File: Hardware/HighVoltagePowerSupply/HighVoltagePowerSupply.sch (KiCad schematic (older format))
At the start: 138 parts, among them J1 Conn_01x02_Female, J10 Conn_01x01_Male, J11 Conn_01x01_Male, J12 Conn_01x01_Male, J13 Conn_01x01_Male, J14 Conn_01x01_Male, J15 Conn_01x03_Female, J16 Conn_01x02_Female, J2 Conn_01x01_Male, J3 Conn_01x01_Male, J4 Conn_01x01_Male, J5 Conn_01x01_Male, J6 Conn_01x01_Male, J7 Conn_01x01_Male, J8 Conn_01x01_Male, J9 Conn_01x01_Male, Q1 BC859, U1 LT3580xMS8E, U3 MCP6V51

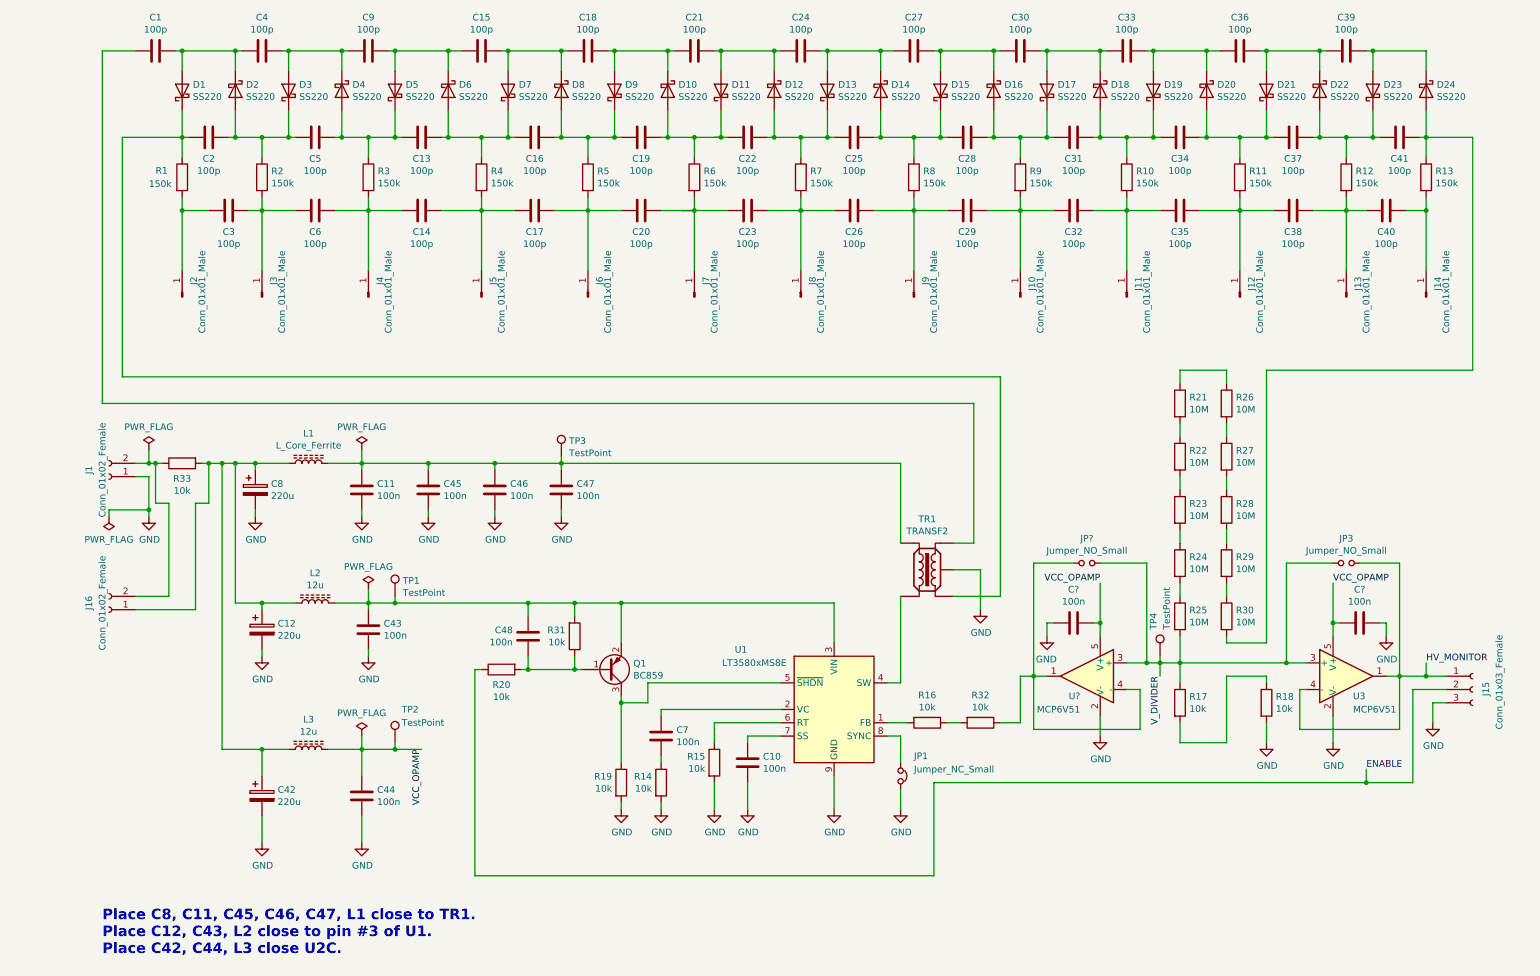
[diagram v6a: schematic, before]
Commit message: 1. GA3459-BL transformwer will be used for hv power supply, added it to the circuit (fix: #7). 2. Status of hv power supply (output voltage, temperature, input current) will be send in an analog way and won't be galvanically isolated (fix: #68) 3. Added missing footprints. 5. Removed obsolete files.
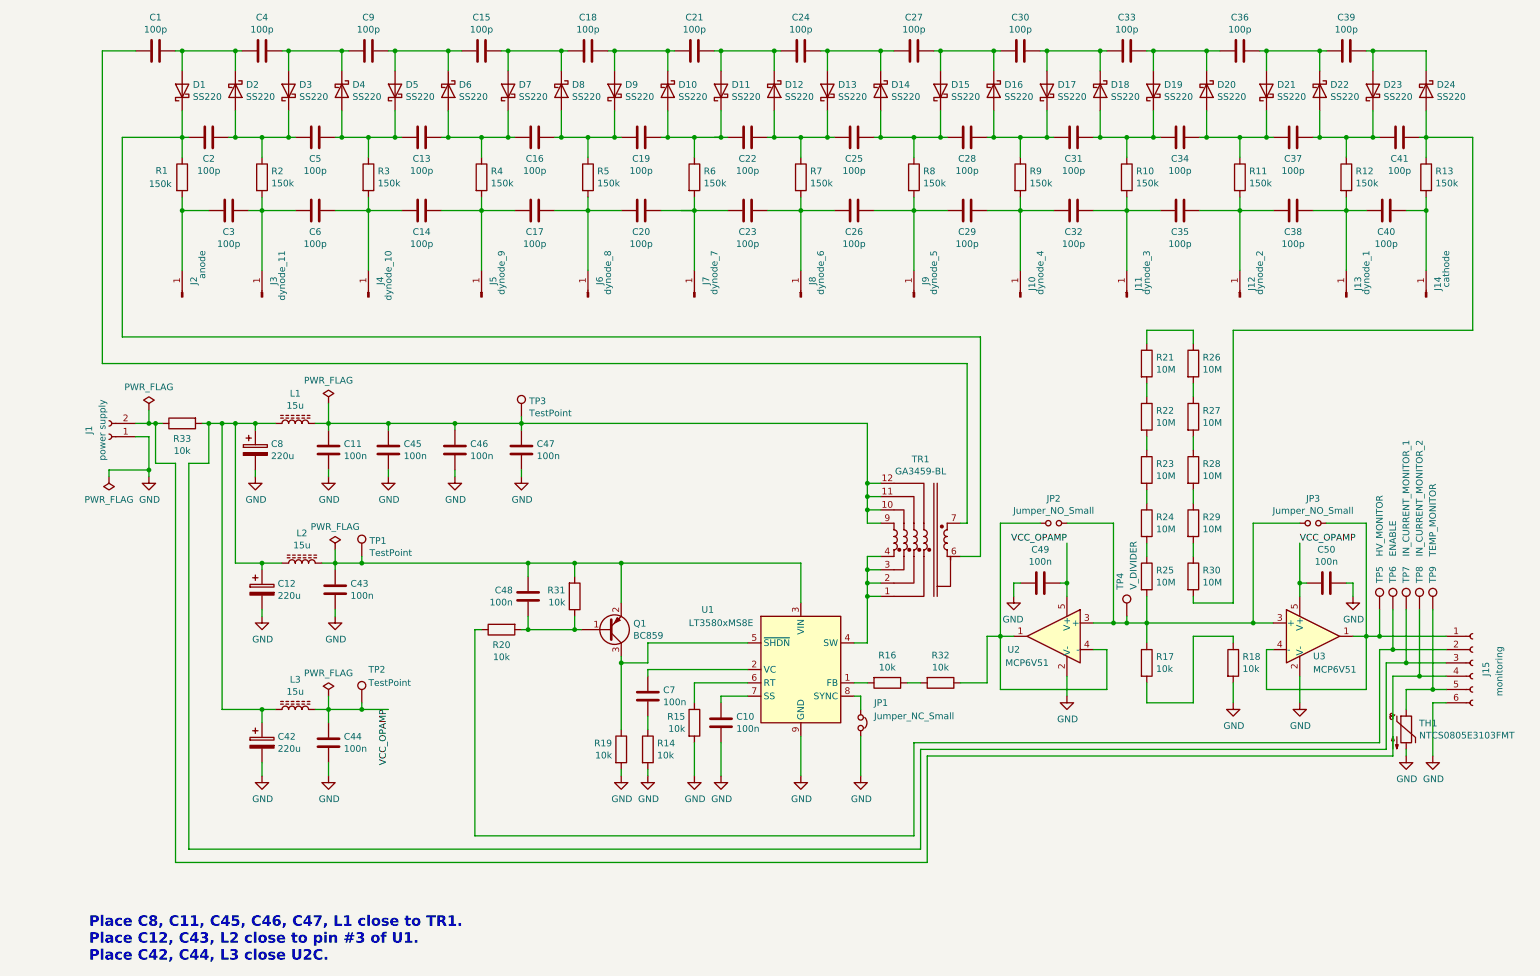
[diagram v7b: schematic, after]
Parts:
- removed J15: Conn_01x03_Female, symbol Connector:Conn_01x03_Female
- removed J16: Conn_01x02_Female, symbol Connector:Conn_01x02_Female
- removed TR1: TRANSF2, symbol Transformer:TRANSF2
- removed U?: MCP6V51, Package_TO_SOT_SMD:SOT-23-5, symbol HighVoltagePowerSupply:MCP6V51
- added J15: monitoring, Connector_PinSocket_2.54mm:PinSocket_1x06_P2.54mm_Vertical, symbol Connector:Conn_01x06_Female
- added TH1: NTCS0805E3103FMT, Resistor_SMD:R_0805_2012Metric, symbol Device:Thermistor_NTC
- added TP5: HV_MONITOR, TestPoint:TestPoint_Pad_D2.5mm, symbol Connector:TestPoint
- added TP6: ENABLE, TestPoint:TestPoint_Pad_D2.5mm, symbol Connector:TestPoint
- added TP7: IN_CURRENT_MONITOR_1, TestPoint:TestPoint_Pad_D2.5mm, symbol Connector:TestPoint
- added TP8: IN_CURRENT_MONITOR_2, TestPoint:TestPoint_Pad_D2.5mm, symbol Connector:TestPoint
- added TP9: TEMP_MONITOR, TestPoint:TestPoint_Pad_D2.5mm, symbol Connector:TestPoint
- added TR1: GA3459-BL, HighVoltagePowerSupply:GA3459-BL, symbol HighVoltagePowerSupply:GA3459-BL
- added U2: MCP6V51, Package_TO_SOT_SMD:SOT-23-5, symbol HighVoltagePowerSupply:MCP6V51
- J1: value Conn_01x02_Female -> power supply; footprint (none) -> HighVoltagePowerSupply:DG300-5.0-02P-12-00A(H)
- J10: value Conn_01x01_Male -> dynode_4
- J11: value Conn_01x01_Male -> dynode_3
- J12: value Conn_01x01_Male -> dynode_2
- J13: value Conn_01x01_Male -> dynode_1
- J14: value Conn_01x01_Male -> cathode
- J2: value Conn_01x01_Male -> anode
- J3: value Conn_01x01_Male -> dynode_11
- J4: value Conn_01x01_Male -> dynode_10
- J5: value Conn_01x01_Male -> dynode_9
- J6: value Conn_01x01_Male -> dynode_8
- J7: value Conn_01x01_Male -> dynode_7
- J8: value Conn_01x01_Male -> dynode_6
- J9: value Conn_01x01_Male -> dynode_5
- L1: value L_Core_Ferrite -> 15u; footprint DataAcquisition:L_7.3x7.3_H3.5 -> HighVoltagePowerSupply:DJNR3015-150
- L2, L3: value 12u -> 15u; footprint DataAcquisition:L_7.3x7.3_H3.5 -> HighVoltagePowerSupply:DJNR3015-150
- TP4: value TestPoint -> V_DIVIDER
- gave numbers to parts that had none: 3
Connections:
- net GND: now also J15.6 (Pin_6), TH1.2, U2.2 (V-)
- net VCC_OPAMP: now also U2.5 (V+)
- net at C1.2: now also TR1.7
- net at C2.2, D1.1 (K), R1.1: now also TR1.6
- net at JP2.2, R32.1: now also U2.1, U2.4 (-)
- net at J1.2 (Pin_2), R33.1: now also J15.4 (Pin_4), TP8.1
- net at C12.1, C42.1, C8.1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: now also J15.3 (Pin_3), TP7.1
- net at U1.4 (SW): now also TR1.1, TR1.2, TR1.3, TR1.4
- net at C11.2, C45.2, C46.2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: now also TR1.10, TR1.11, TR1.12, TR1.9
- net ENABLE: no longer names the net of R20.1
- net ENABLE: now also J15.2 (Pin_2), TP6.1
- net HV_MONITOR: no longer names the net of JP3.2, U3.1, U3.4 (-)
- net HV_MONITOR: now also J15.1 (Pin_1), TP5.1
- net V_DIVIDER: no longer names the net of JP2.1, JP3.1, R17.1, R25.2, TP4.1, U3.3 (+)
- net V_DIVIDER: now also U2.3 (+)
- new net: J15.5 (Pin_5), TH1.1, TP9.1
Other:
- moved on the sheet: C10, C11, C12, C42, C43, C44, C45, C46, C47, C48, C49, C50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

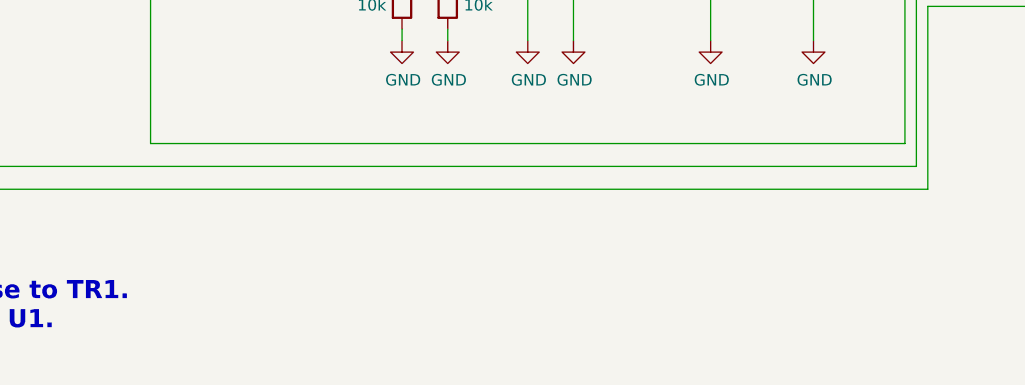
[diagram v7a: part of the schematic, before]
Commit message: Chose correct PCB outlines based on mechanical overview (fix: #50).
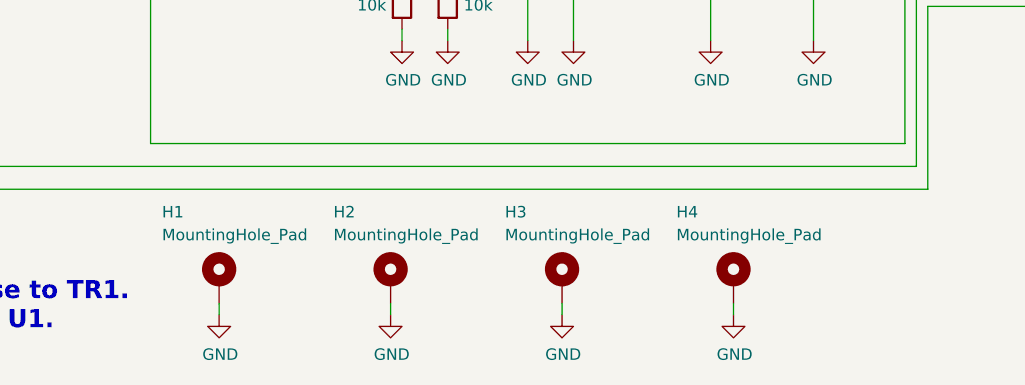
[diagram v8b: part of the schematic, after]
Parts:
- added H1, H2, H3, H4: MountingHole_Pad, MountingHole:MountingHole_3.5mm_Pad, symbol Mechanical:MountingHole_Pad
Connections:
- net GND: now also H1.1, H2.1, H3.1, H4.1
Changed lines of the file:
@@
 	0    -1   -1   0
 $EndComp
+$Comp
+L Mechanical:MountingHole_Pad H1
+U 1 1 5FF355F1
+P 3750 7400
+F 0 "H1" H 3500 7700 50  0000 L CNN
+F 1 "MountingHole_Pad" H 3500 7600 50  0000 L CNN
+F 2 "MountingHole:MountingHole_3.5mm_Pad" H 3750 7400 50  0001 C CNN
+F 3 "~" H 3750 7400 50  0001 C CNN
+	1    3750 7400
+	1    0    0    -1
+$EndComp
+$Comp
+L power:GND #PWR?
+U 1 1 5FF355F7
+P 3750 7550
+AR Path="/5EDA53F3/5FF355F7" Ref="#PWR?"  Part="1"
+AR Path="/5EDA5628/5FF355F7" Ref="#PWR?"  Part="1"
+AR Path="/5FF355F7" Ref="#PWR023"  Part="1"
+F 0 "#PWR023" H 3750 7300 50  0001 C CNN
+F 1 "GND" H 3755 7377 50  0000 C CNN
+F 2 "" H 3750 7550 50  0001 C CNN
+F 3 "" H 3750 7550 50  0001 C CNN
+	1    3750 7550
+	1    0    0    -1
+$EndComp
+Wire Wire Line
+	3750 7500 3750 7550
+$Comp
+L Mechanical:MountingHole_Pad H2
+U 1 1 6001BF81
+P 4500 7400
+F 0 "H2" H 4250 7700 50  0000 L CNN
+F 1 "MountingHole_Pad" H 4250 7600 50  0000 L CNN
+F 2 "MountingHole:MountingHole_3.5mm_Pad" H 4500 7400 50  0001 C CNN
+F 3 "~" H 4500 7400 50  0001 C CNN
+	1    4500 7400
+	1    0    0    -1
+$EndComp
+$Comp
+L power:GND #PWR?
+U 1 1 6001BF87
+P 4500 7550
+AR Path="/5EDA53F3/6001BF87" Ref="#PWR?"  Part="1"
+AR Path="/5EDA5628/6001BF87" Ref="#PWR?"  Part="1"
+AR Path="/6001BF87" Ref="#PWR024"  Part="1"
+F 0 "#PWR024" H 4500 7300 50  0001 C CNN
+F 1 "GND" H 4505 7377 50  0000 C CNN
+F 2 "" H 4500 7550 50  0001 C CNN
+F 3 "" H 4500 7550 50  0001 C CNN
+	1    4500 7550
+	1    0    0    -1
+$EndComp
+Wire Wire Line
+	4500 7500 4500 7550
+$Comp
+L Mechanical:MountingHole_Pad H3
+U 1 1 6004886A
+P 5250 7400
+F 0 "H3" H 5000 7700 50  0000 L CNN
+F 1 "MountingHole_Pad" H 5000 7600 50  0000 L CNN
+F 2 "MountingHole:MountingHole_3.5mm_Pad" H 5250 7400 50  0001 C CNN
+F 3 "~" H 5250 7400 50  0001 C CNN
+	1    5250 7400
+	1    0    0    -1
+$EndComp
+$Comp
+L power:GND #PWR?
+U 1 1 60048870
+P 5250 7550
+AR Path="/5EDA53F3/60048870" Ref="#PWR?"  Part="1"
+AR Path="/5EDA5628/60048870" Ref="#PWR?"  Part="1"
+AR Path="/60048870" Ref="#PWR025"  Part="1"
+F 0 "#PWR025" H 5250 7300 50  0001 C CNN
+F 1 "GND" H 5255 7377 50  0000 C CNN
+F 2 "" H 5250 7550 50  0001 C CNN
+F 3 "" H 5250 7550 50  0001 C CNN
+	1    5250 7550
+	1    0    0    -1
+$EndComp
+Wire Wire Line
+	5250 7500 5250 7550
+$Comp
+L Mechanical:MountingHole_Pad H4
+U 1 1 600757CC
+P 6000 7400
+F 0 "H4" H 5750 7700 50  0000 L CNN
+F 1 "MountingHole_Pad" H 5750 7600 50  0000 L CNN
+F 2 "MountingHole:MountingHole_3.5mm_Pad" H 6000 7400 50  0001 C CNN
+F 3 "~" H 6000 7400 50  0001 C CNN
+	1    6000 7400
+	1    0    0    -1
+$EndComp
+$Comp
+L power:GND #PWR?
+U 1 1 600757D2
+P 6000 7550
+AR Path="/5EDA53F3/600757D2" Ref="#PWR?"  Part="1"
+AR Path="/5EDA5628/600757D2" Ref="#PWR?"  Part="1"
+AR Path="/600757D2" Ref="#PWR026"  Part="1"
+F 0 "#PWR026" H 6000 7300 50  0001 C CNN
+F 1 "GND" H 6005 7377 50  0000 C CNN
+F 2 "" H 6000 7550 50  0001 C CNN
+F 3 "" H 6000 7550 50  0001 C CNN
+	1    6000 7550
+	1    0    0    -1
+$EndComp
+Wire Wire Line
+	6000 7500 6000 7550
 $EndSCHEMATC
